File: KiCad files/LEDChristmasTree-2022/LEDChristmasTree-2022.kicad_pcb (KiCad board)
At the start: 2 copper layers, 74.9 x 99.2 mm, 24 parts, among them SW1 SW_SPDT

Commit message: layout
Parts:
- added D12: RGB, Library:LED-0807, F.Cu at (127.7, 109.6)
- added R12: 2k, Resistor_SMD:R_0603_1608Metric, B.Cu at (158.0, 109.6)
- moved R2 36.8 mm to (158.0, 113.8)
- moved R6 10.2 mm to (159.8, 118.4)
- moved D7 9.76 mm to (164.7, 118.4)
- moved D10 6.26 mm to (131.6, 93.1)
- moved D4 6.23 mm to (150.1, 85.6)
- moved D5 6.18 mm to (152.6, 122.9)
- moved R5 6.10 mm to (158.0, 122.9)
- moved R3 6.00 mm to (158.0, 125.4)
- moved D3 5.67 mm to (133.5, 125.0)
- moved D8 3.18 mm to (156.1, 99.9)
- moved R7 3.06 mm to (161.0, 100.4)
- moved R8 2.70 mm to (128.3, 97.0)
- moved D1 1.48 mm to (142.9, 105.8)
- moved R1 1.40 mm to (158.0, 105.8)
- moved D6 1.39 mm to (145.9, 66.1)
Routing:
- net Net-(R1-Pad1): track 219.6 -> 62.3 mm
- net unconnected-(BT1-Pad2): track 45.0 -> 0.00 mm
- net Net-(D2-Pad1): track 5.07 -> 44.8 mm
- net Net-(D12-Pad1): track 0.00 -> 30.1 mm, vias 0 -> 1
- net Net-(D11-Pad1): track 23.1 -> 0.00 mm, vias 1 -> 0
- net Net-(D4-Pad1): track 15.8 -> 0.00 mm, vias 1 -> 0
- net Net-(D10-Pad1): track 10.3 -> 0.00 mm, vias 1 -> 0
- net Net-(D8-Pad1): track 9.41 -> 0.00 mm, vias 1 -> 0
- net Net-(D6-Pad1): track 6.28 -> 0.00 mm, vias 1 -> 0
- net Net-(D9-Pad1): track 4.67 -> 0.00 mm, vias 1 -> 0
- net VCC: track 29.1 -> 25.7 mm
- net Net-(D3-Pad1): track 22.9 -> 24.6 mm
- net Net-(D1-Pad1): track 15.4 -> 14.4 mm
- net Net-(D5-Pad1): track 3.67 -> 4.67 mm
- net Net-(D7-Pad1): track 3.47 -> 4.17 mm
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
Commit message: layout
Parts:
- moved R2 37.2 mm to (122.5, 125.0)
- moved R12 29.8 mm to (128.3, 112.8)
- moved R3 29.7 mm to (128.3, 125.0), turned to 0 degrees
- moved R7 2.75 mm to (159.5, 102.7)
- moved R4 2.42 mm to (159.5, 96.1)
- moved R1 1.50 mm to (159.5, 105.8)
- moved R5 1.50 mm to (159.5, 122.9)
- moved D2 0.90 mm to (117.2, 126.1)
- moved R9 0.68 mm to (128.3, 103.4)
- moved R6 0.30 mm to (159.5, 118.4)
- turned R8 to 0 degrees
- turned D12 to 0 degrees
- turned D3 to 0 degrees
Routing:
- net Net-(R1-Pad1): track 62.3 -> 216.8 mm
- net unconnected-(BT1-Pad2): track 0.00 -> 51.9 mm
- net Net-(D2-Pad1): track 44.8 -> 5.02 mm
- net Net-(D11-Pad1): track 0.00 -> 28.0 mm, vias 0 -> 1
- net Net-(D3-Pad1): track 24.6 -> 4.44 mm
- net Net-(D12-Pad1): track 30.1 -> 10.9 mm
- net Net-(D10-Pad1): track 0.00 -> 18.0 mm, vias 0 -> 1
- net Net-(D4-Pad1): track 0.00 -> 16.7 mm, vias 0 -> 1
- net Net-(D8-Pad1): track 0.00 -> 8.23 mm, vias 0 -> 1
- net Net-(D6-Pad1): track 0.00 -> 4.83 mm, vias 0 -> 1
- net Net-(D9-Pad1): track 0.00 -> 4.67 mm, vias 0 -> 1
- net Net-(D5-Pad1): track 4.67 -> 6.17 mm
- net Net-(D1-Pad1): track 14.4 -> 15.9 mm
- net GND: vias 13 -> 21

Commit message: up
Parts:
- added G***: LOGO, Library:snowflake, F.Cu at (141.2, 92.7)
- added G***: LOGO, Library:snowflake, F.Cu at (135.1, 114.0)
- added G***: LOGO, Library:snowflake, F.Cu at (166.6, 126.2)
- added G***: LOGO, Library:snowflake, F.Cu at (125.4, 123.5)
- added G***: LOGO, Library:snowflake, F.Cu at (147.4, 128.3)
- added G***: LOGO, Library:snowflake, F.Cu at (146.7, 74.1)
- added G***: LOGO, Library:snowflake, F.Cu at (138.8, 66.1)
- added G***: LOGO, Library:snowflake, F.Cu at (148.2, 100.2)

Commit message: gerber
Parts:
- added G***: LOGO, Library:candy_cane, F.Cu at (132.0, 105.3)
- added G***: LOGO, Library:candy_cane, F.Cu at (131.5, 79.4)
- added G***: LOGO, Library:candy_cane, F.Cu at (142.1, 123.6)
- added G***: LOGO, Library:logo, B.Cu at (173.0, 126.0)
- added G***: LOGO, Library:candy_cane, F.Cu at (144.0, 91.2)
- added G***: LOGO, Library:snowflake, F.Cu at (163.3, 100.0)
- added G***: LOGO, Library:candy_cane, F.Cu at (164.4, 124.4)
- added G***: LOGO, Library:candy_cane, F.Cu at (152.1, 107.6)
- moved G*** 6.64 mm to (135.5, 89.3)
- moved G*** 6.61 mm to (173.2, 125.9)
- moved G*** 1.14 mm to (134.8, 112.9)

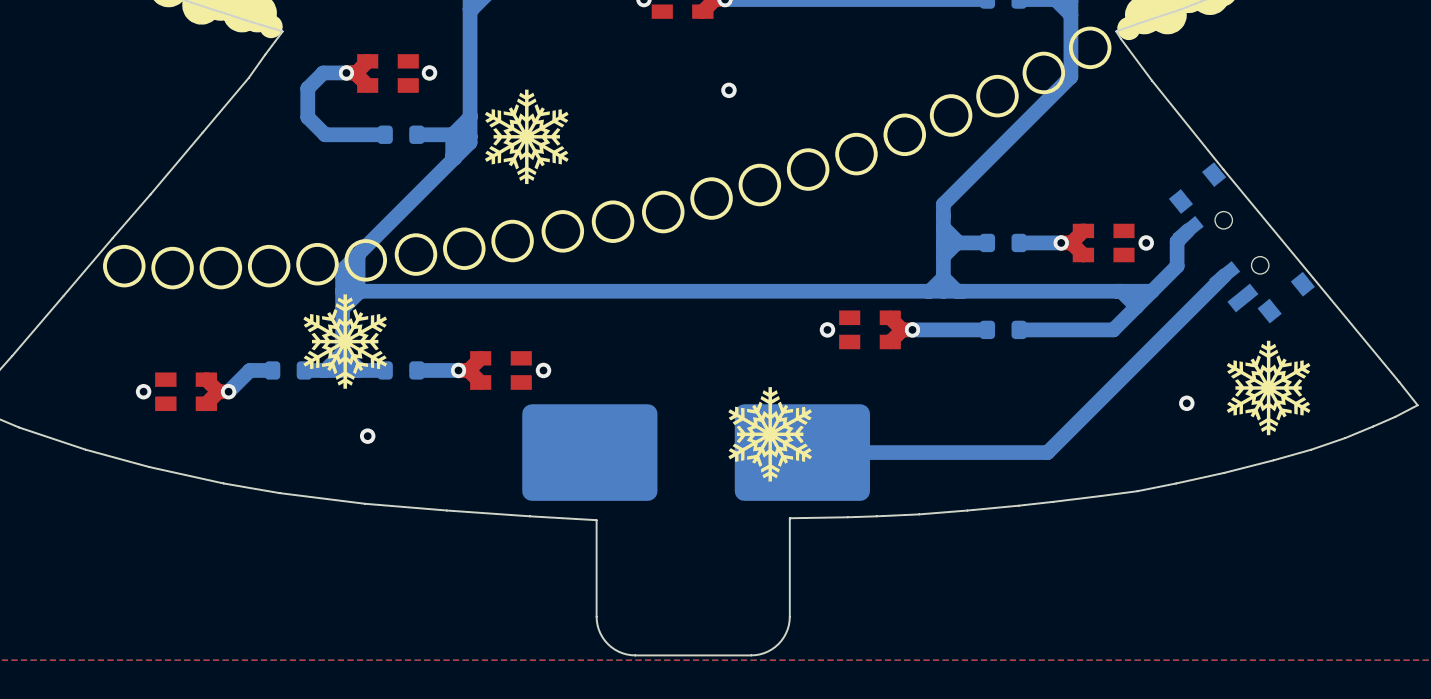
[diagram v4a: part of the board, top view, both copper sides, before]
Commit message: fixed battery polarity
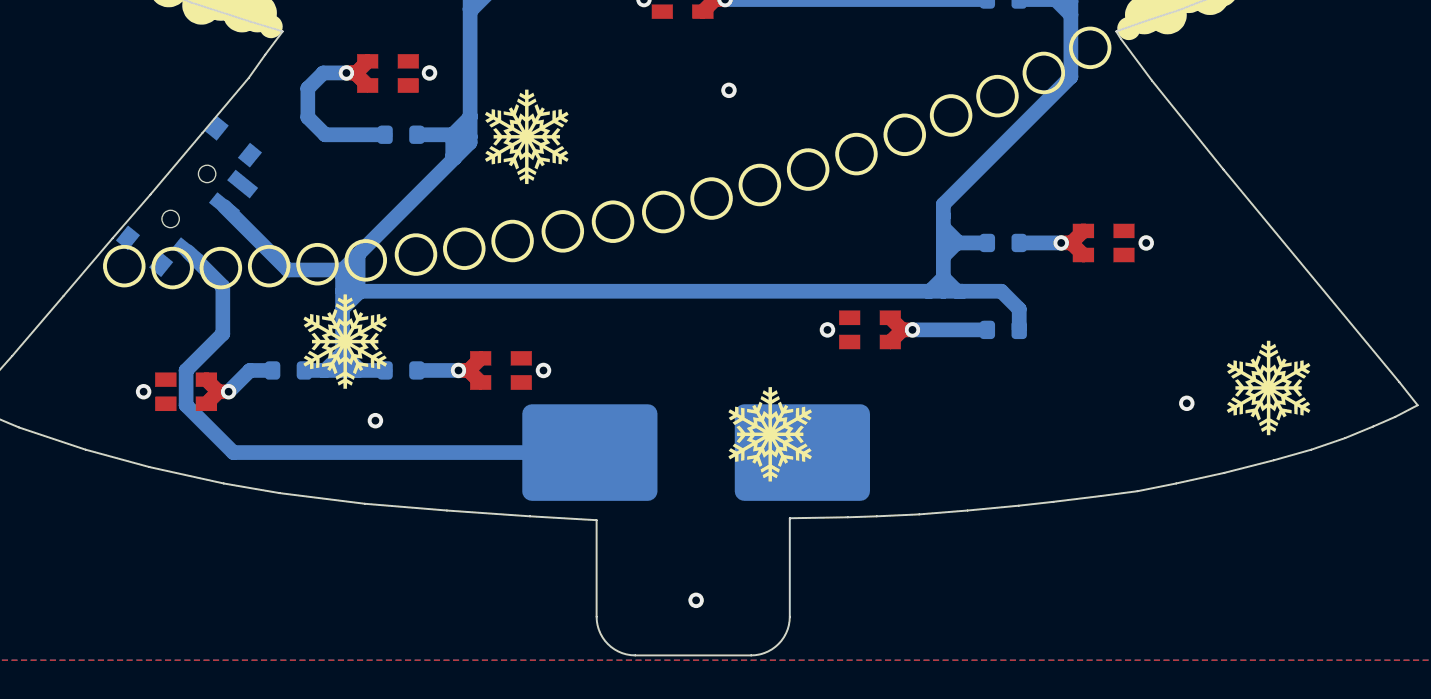
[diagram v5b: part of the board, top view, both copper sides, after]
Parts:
- moved SW1 54.1 mm to (117.6, 116.2), turned to 51 degrees
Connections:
- BT1 pad 1: VCC -> GND
- BT1 pad 3: GND -> VCC
- SW1 pad 1: Net-(R1-Pad1) -> VCC
- SW1 pad 2: VCC -> Net-(R1-Pad1)
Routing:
- net Net-(R1-Pad1): track 216.8 -> 205.9 mm
- net VCC: track 25.7 -> 31.4 mm
- net GND: vias 21 -> 22
